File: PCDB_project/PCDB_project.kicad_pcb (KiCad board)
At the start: 4 copper layers, 100 x 80 mm, 59 parts, among them J1 Power, J2 22-05-7025, J3 22-05-7025, J4 22-05-7025, J5 22-05-7025, J6 Comm, J7 USB_B_Mini, J8 Debug, M1 BSS84, M2 BSS84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

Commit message: Placement acabado pero hay algunas dudas que resolver con el profe
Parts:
- added FD1: Fiducial_1mm_Mask3mm, Fiducial:Fiducial_1mm_Mask3mm, F.Cu at (10.0, 70.0)
- added FD2: Fiducial_1mm_Mask3mm, Fiducial:Fiducial_1mm_Mask3mm, F.Cu at (90.0, 70.0)
- added FD3: Fiducial_1mm_Mask3mm, Fiducial:Fiducial_1mm_Mask3mm, F.Cu at (90.0, 10.0)
- added H1: MountingHole_3.2mm_M3, MountingHole:MountingHole_3.2mm_M3, F.Cu at (5.00, 5.00)
- added H2: MountingHole_3.2mm_M3, MountingHole:MountingHole_3.2mm_M3, F.Cu at (95.0, 5.00)
- added H3: MountingHole_3.2mm_M3, MountingHole:MountingHole_3.2mm_M3, F.Cu at (5.00, 75.0)
- added H4: MountingHole_3.2mm_M3, MountingHole:MountingHole_3.2mm_M3, F.Cu at (95.0, 75.0)
- moved R7 247.0 mm to (10.5, 35.0), turned to 90 degrees
- moved M2 239.4 mm to (30.0, 34.6), turned to 180 degrees
- moved R6 238.0 mm to (25.4, 34.9), turned to 270 degrees
- moved C14 236.8 mm to (29.0, 47.3), turned to 180 degrees
- moved MOV2 235.2 mm to (22.2, 42.4), turned to 180 degrees
- moved U5 228.8 mm to (32.2, 43.4), turned to 180 degrees
- moved MOV3 223.6 mm to (22.2, 46.7), turned to 180 degrees
- moved R3 213.9 mm to (19.0, 65.0), turned to 270 degrees
- moved R2 199.0 mm to (11.7, 56.3), turned to 270 degrees
- moved R11 195.2 mm to (47.6, 59.1), turned to 180 degrees
- moved C8 194.6 mm to (44.4, 46.3)
- moved M1 191.4 mm to (84.0, 11.5), turned to 270 degrees
- moved L1 189.4 mm to (15.5, 11.5)
- moved C6 187.2 mm to (51.2, 59.1), turned to 180 degrees
- moved U4 186.7 mm to (78.8, 21.0), turned to 90 degrees
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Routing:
- net V_USB: track 0.00 -> 79.7 mm
- net Net-(LD2-Pad1): track 0.00 -> 53.1 mm
- net GATE: track 0.00 -> 44.3 mm
- net Net-(U3-Pad17): track 0.00 -> 42.1 mm
- net FAN2_C: track 0.00 -> 35.3 mm
- net USB_DM: track 0.00 -> 34.9 mm
- net USB_DP: track 0.00 -> 34.9 mm
- net DIR: track 0.00 -> 26.8 mm
- net TX: track 0.00 -> 25.1 mm
- net Net-(J6-Pad1): track 0.00 -> 24.6 mm
- net Net-(J6-Pad3): track 0.00 -> 23.0 mm
- net RX: track 0.00 -> 19.1 mm
- net SWDIO: track 0.00 -> 19.0 mm
- net FAN1_C: track 0.00 -> 16.4 mm
- net ALARM_C: track 0.00 -> 16.0 mm
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
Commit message: Correciones profe
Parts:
- moved C12 20.1 mm to (39.8, 64.6)
- moved R7 17.6 mm to (25.9, 43.5)
- moved MOV2 15.5 mm to (10.4, 32.4), turned to 90 degrees
- moved MOV3 14.0 mm to (11.7, 37.5), turned to 270 degrees
- moved J8 7.45 mm to (50.0, 72.8), turned to 0 degrees
- moved M2 3.93 mm to (33.9, 34.1)
- moved R6 2.65 mm to (28.0, 34.4), turned to 180 degrees
- moved X1 0.20 mm to (60.5, 55.7)
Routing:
- net Net-(LD2-Pad1): track 53.1 -> 26.1 mm
- net Net-(U3-Pad17): track 42.1 -> 54.3 mm
- net FAN2_C: track 35.3 -> 47.1 mm
- net GATE: track 44.3 -> 55.7 mm
- net SWDIO: track 19.0 -> 28.7 mm
- net Net-(C11-Pad1): track 2.36 -> 9.65 mm
- net Net-(C10-Pad1): track 4.62 -> 10.5 mm
- net DIR: track 26.8 -> 31.5 mm
- net SWCLK: track 12.0 -> 15.6 mm
- net Net-(J6-Pad3): track 23.0 -> 26.6 mm
- net TX: track 25.1 -> 21.9 mm
- net Net-(J6-Pad1): track 24.6 -> 21.6 mm

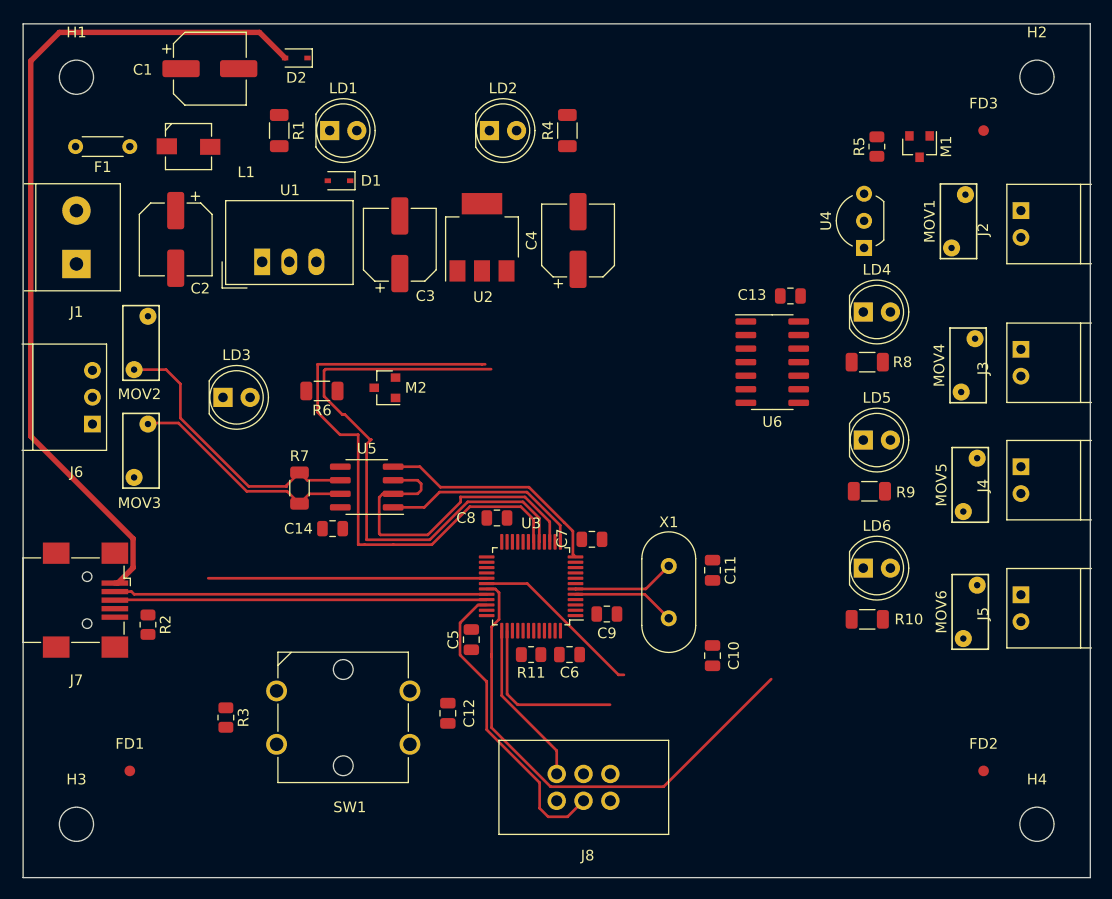
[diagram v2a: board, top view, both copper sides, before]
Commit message: Enrutado conseguido pero hay alguna cosa que no me acab de gustar, nrst y chip de puertas logicas
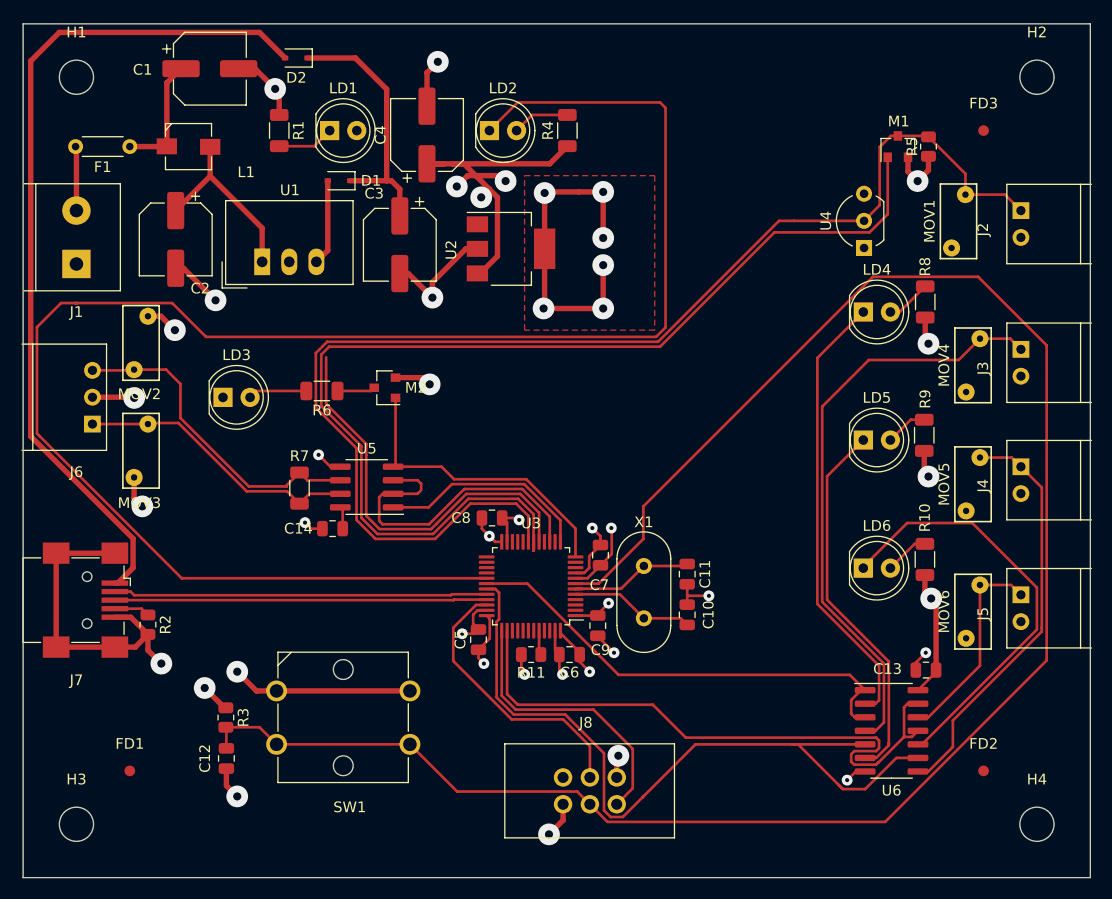
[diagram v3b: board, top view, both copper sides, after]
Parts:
- U6: value MC74LCX0 -> MC74LCX07
- moved C13 37.3 mm to (84.6, 60.6)
- moved U6 36.3 mm to (81.4, 66.2)
- moved C12 21.2 mm to (19.1, 68.8), turned to 270 degrees
- moved C4 17.3 mm to (37.8, 10.4)
- moved R8 7.83 mm to (84.5, 26.1), turned to 90 degrees
- moved R10 7.79 mm to (84.5, 50.2), turned to 90 degrees
- moved R9 7.34 mm to (84.4, 38.6), turned to 90 degrees
- moved J8 6.04 mm to (55.6, 70.6), turned to 180 degrees
- moved R5 4.84 mm to (84.8, 11.5), turned to 270 degrees
- moved C10 4.50 mm to (62.2, 55.4)
- moved U2 2.93 mm to (45.7, 21.1), turned to 0 degrees
- moved C11 2.40 mm to (62.2, 51.6)
- moved X1 2.33 mm to (58.2, 55.7)
- moved M1 2.03 mm to (82.0, 11.5), turned to 90 degrees
- moved C7 1.69 mm to (54.1, 49.8), turned to 270 degrees
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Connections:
- J7 pad 5: Net-(J7-Pad5) -> GND
- J7 pad 6: Net-(J7-Pad5) -> GND
- R2 pad 2: Net-(J7-Pad5) -> GND
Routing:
- net NRST: track 0.00 -> 178.9 mm
- net GND: track 0.00 -> 158.6 mm, vias 0 -> 28
- net Net-(LD2-Pad1): track 26.1 -> 157.9 mm
- net DQ: track 0.00 -> 120.2 mm
- net +3V3: track 0.00 -> 92.8 mm, vias 0 -> 15
- net Net-(J3-Pad1): track 0.00 -> 55.7 mm
- net GATE: track 55.7 -> 103.8 mm
- net ALARM_C: track 16.0 -> 59.5 mm
- net Net-(LD4-Pad1): track 0.00 -> 42.0 mm
- net Net-(LD6-Pad1): track 0.00 -> 40.1 mm
- net Net-(J4-Pad1): track 0.00 -> 38.9 mm
- net Net-(LD5-Pad1): track 0.00 -> 36.6 mm
- net FAN1_C: track 16.4 -> 44.0 mm
- net /Supply/pwr5: track 0.00 -> 24.7 mm
- net FAN2_C: track 47.1 -> 71.7 mm
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- added copper zone on F.Cu, net GND

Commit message: Proyecto basico acabado, hay que preguntar al profe un par de cosas mas del proyecto baisco para cerrarlo definitivamente
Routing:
- net (no net): track 0.00 -> 27.8 mm
- net GND: track 158.6 -> 138.3 mm, vias 28 -> 26
- net V_USB: track 79.7 -> 70.9 mm
- net Net-(LD2-Pad1): track 157.9 -> 152.8 mm
- net +3V3: track 92.8 -> 90.7 mm, vias 15 -> 14
- added copper zone on In2.Cu, net +3V3
- added copper zone on B.Cu, net GND
- added copper zone on In1.Cu, net GND
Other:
- board text added: "PCBD Project v1.0"
